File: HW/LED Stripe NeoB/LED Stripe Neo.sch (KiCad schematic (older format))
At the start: 22 parts, among them J1 IN-OUT, J2 IN-OUT, U1 WS2812B, U10 WS2812B, U2 WS2812B, U3 WS2812B, U4 WS2812B, U5 WS2812B, U6 WS2812B, U7 WS2812B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

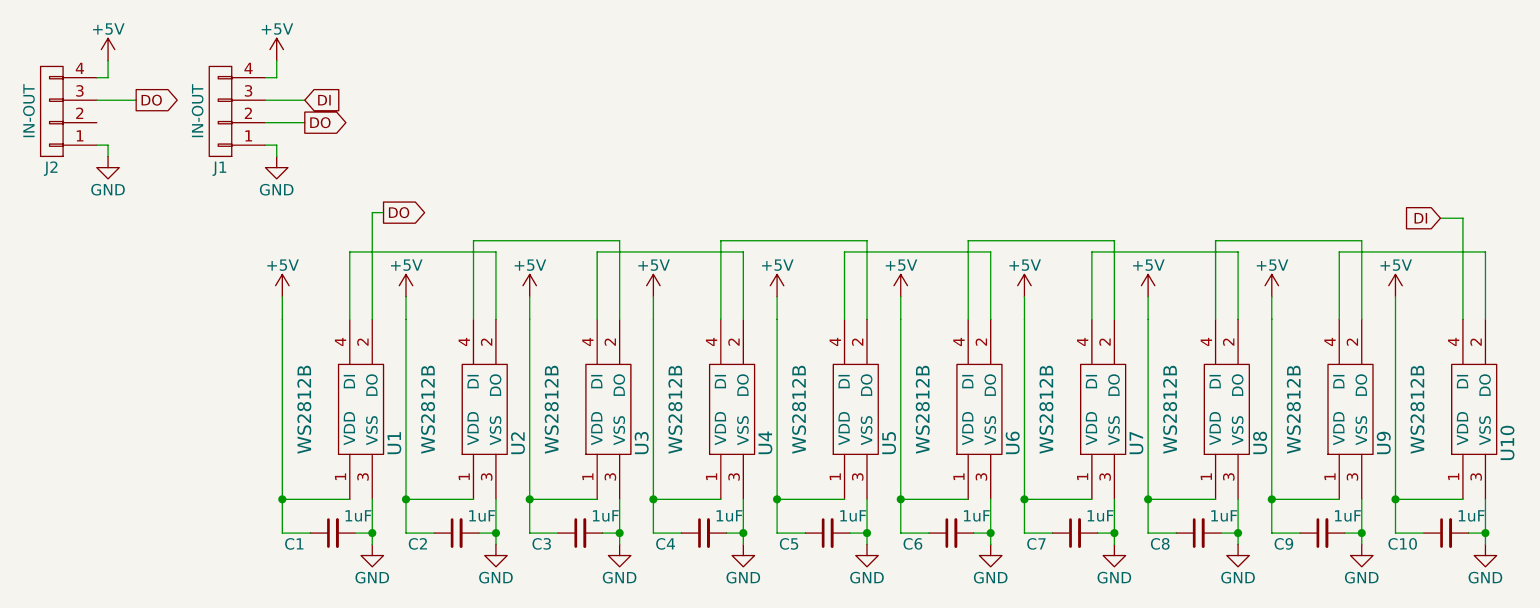
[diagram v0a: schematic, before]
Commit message: WS2812B SCH/PCB added
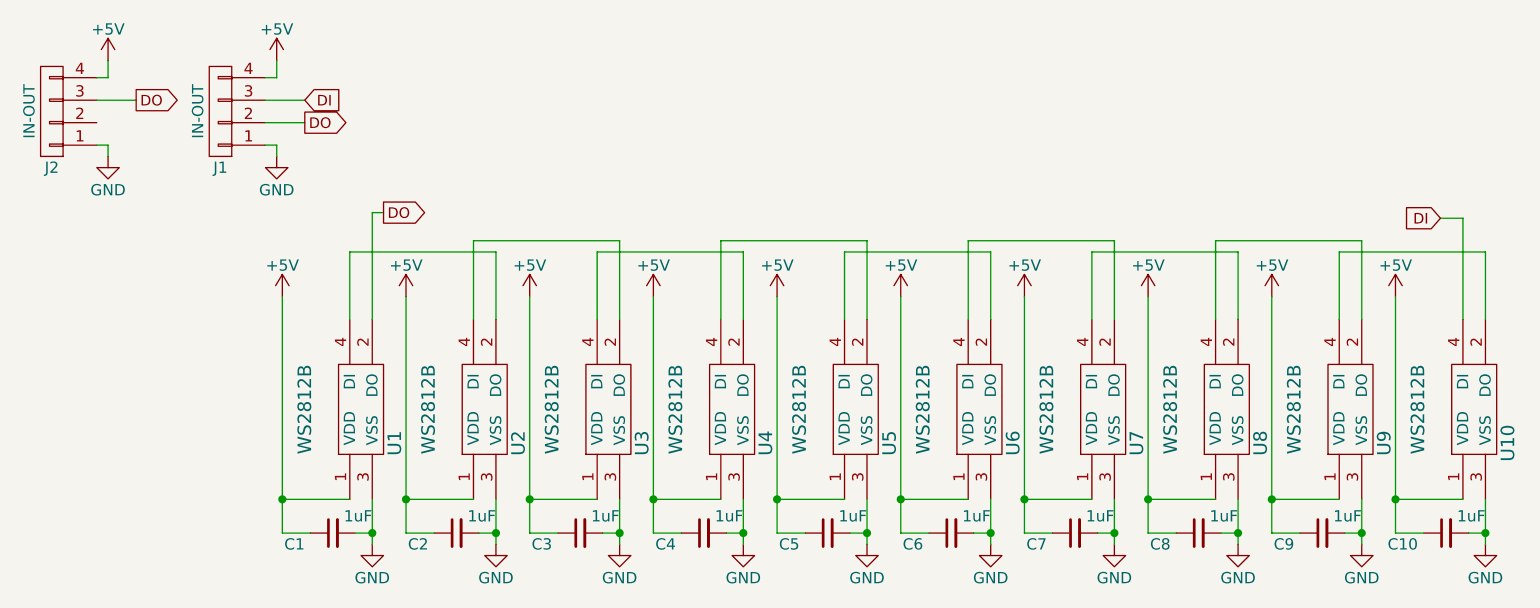
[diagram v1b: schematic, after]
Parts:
- U1, U10, U2, U3, U4, U5, U6, U7, U8, U9: footprint LEDs:LED-RGB_PLLC-6 -> suf_led:LED5050-WS2812B_HANDSOLDERING
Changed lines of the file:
@@
 LIBS:valves
 LIBS:suf_led
+LIBS:LED Stripe Neo-cache
 EELAYER 25 0
 EELAYER END
@@
 F 0 "U1" H 2000 2100 60  0000 C CNN
 F 1 "WS2812B" H 2150 2500 60  0000 C CNN
-F 2 "LEDs:LED-RGB_PLLC-6" H 2150 2300 60  0001 C CNN
+F 2 "suf_led:LED5050-WS2812B_HANDSOLDERING" H 2150 2300 60  0001 C CNN
 F 3 "" H 2150 2300 60  0000 C CNN
 	1    2150 2300
@@
 $EndComp
 Wire Wire Line
-	1850 1800 1850 1900
-Wire Wire Line
-	1850 1900 1850 2700
-Wire Wire Line
-	1850 2700 1850 2850
+	1850 1800 1850 2850
 Wire Wire Line
 	1850 2700 2150 2700
@@
 $EndComp
 Wire Wire Line
-	2250 2700 2250 2850
-Wire Wire Line
-	2250 2850 2250 2900
+	2250 2700 2250 2900
 Wire Wire Line
 	2175 2850 2250 2850
@@
 F 0 "U2" H 2550 2100 60  0000 C CNN
 F 1 "WS2812B" H 2700 2500 60  0000 C CNN
-F 2 "LEDs:LED-RGB_PLLC-6" H 2700 2300 60  0001 C CNN
+F 2 "suf_led:LED5050-WS2812B_HANDSOLDERING" H 2700 2300 60  0001 C CNN
 F 3 "" H 2700 2300 60  0000 C CNN
 	1    2700 2300
@@
 $EndComp
 Wire Wire Line
-	2400 1800 2400 1900
-Wire Wire Line
-	2400 1900 2400 2700
-Wire Wire Line
-	2400 2700 2400 2850
+	2400 1800 2400 2850
 Wire Wire Line
 	2400 2700 2700 2700
@@
 $EndComp
 Wire Wire Line
-	2800 2700 2800 2850
-Wire Wire Line
-	2800 2850 2800 2900
+	2800 2700 2800 2900
 Wire Wire Line
 	2725 2850 2800 2850
@@
 F 0 "U3" H 3100 2100 60  0000 C CNN
 F 1 "WS2812B" H 3250 2500 60  0000 C CNN
-F 2 "LEDs:LED-RGB_PLLC-6" H 3250 2300 60  0001 C CNN
+F 2 "suf_led:LED5050-WS2812B_HANDSOLDERING" H 3250 2300 60  0001 C CNN
 F 3 "" H 3250 2300 60  0000 C CNN
 	1    3250 2300
@@
 $EndComp
 Wire Wire Line
-	2950 1800 2950 1900
-Wire Wire Line
-	2950 1900 2950 2700
-Wire Wire Line
-	2950 2700 2950 2850
+	2950 1800 2950 2850
 Wire Wire Line
 	2950 2700 3250 2700
@@
 $EndComp
 Wire Wire Line
-	3350 2700 3350 2850
-Wire Wire Line
-	3350 2850 3350 2900
+	3350 2700 3350 2900
 Wire Wire Line
 	3275 2850 3350 2850
@@
 F 0 "U4" H 3650 2100 60  0000 C CNN
 F 1 "WS2812B" H 3800 2500 60  0000 C CNN
-F 2 "LEDs:LED-RGB_PLLC-6" H 3800 2300 60  0001 C CNN
+F 2 "suf_led:LED5050-WS2812B_HANDSOLDERING" H 3800 2300 60  0001 C CNN
 F 3 "" H 3800 2300 60  0000 C CNN
 	1    3800 2300
@@
 $EndComp
 Wire Wire Line
-	3500 1800 3500 1900
-Wire Wire Line
-	3500 1900 3500 2700
-Wire Wire Line
-	3500 2700 3500 2850
+	3500 1800 3500 2850
 Wire Wire Line
 	3500 2700 3800 2700
@@
 $EndComp
 Wire Wire Line
-	3900 2700 3900 2850
-Wire Wire Line
-	3900 2850 3900 2900
+	3900 2700 3900 2900
 Wire Wire Line
 	3825 2850 3900 2850
@@
 F 0 "U5" H 4200 2100 60  0000 C CNN
 F 1 "WS2812B" H 4350 2500 60  0000 C CNN
-F 2 "LEDs:LED-RGB_PLLC-6" H 4350 2300 60  0001 C CNN
+F 2 "suf_led:LED5050-WS2812B_HANDSOLDERING" H 4350 2300 60  0001 C CNN
 F 3 "" H 4350 2300 60  0000 C CNN
 	1    4350 2300
@@
 $EndComp
 Wire Wire Line
-	4050 1800 4050 1900
-Wire Wire Line
-	4050 1900 4050 2700
-Wire Wire Line
-	4050 2700 4050 2850
+	4050 1800 4050 2850
 Wire Wire Line
 	4050 2700 4350 2700
@@
 $EndComp
 Wire Wire Line
-	4450 2700 4450 2850
-Wire Wire Line
-	4450 2850 4450 2900
+	4450 2700 4450 2900
 Wire Wire Line
 	4375 2850 4450 2850
@@
 F 0 "U6" H 4750 2100 60  0000 C CNN
 F 1 "WS2812B" H 4900 2500 60  0000 C CNN
-F 2 "LEDs:LED-RGB_PLLC-6" H 4900 2300 60  0001 C CNN
+F 2 "suf_led:LED5050-WS2812B_HANDSOLDERING" H 4900 2300 60  0001 C CNN
 F 3 "" H 4900 2300 60  0000 C CNN
 	1    4900 2300
@@
 $EndComp
 Wire Wire Line
-	4600 1800 4600 1900
-Wire Wire Line
-	4600 1900 4600 2700
-Wire Wire Line
-	4600 2700 4600 2850
+	4600 1800 4600 2850
 Wire Wire Line
 	4600 2700 4900 2700
@@
 $EndComp
 Wire Wire Line
-	5000 2700 5000 2850
-Wire Wire Line
-	5000 2850 5000 2900
+	5000 2700 5000 2900
 Wire Wire Line
 	4925 2850 5000 2850
@@
 F 0 "U7" H 5300 2100 60  0000 C CNN
 F 1 "WS2812B" H 5450 2500 60  0000 C CNN
-F 2 "LEDs:LED-RGB_PLLC-6" H 5450 2300 60  0001 C CNN
+F 2 "suf_led:LED5050-WS2812B_HANDSOLDERING" H 5450 2300 60  0001 C CNN
 F 3 "" H 5450 2300 60  0000 C CNN
 	1    5450 2300
@@
 $EndComp
 Wire Wire Line
-	5150 1800 5150 1900
-Wire Wire Line
-	5150 1900 5150 2700
-Wire Wire Line
-	5150 2700 5150 2850
+	5150 1800 5150 2850
 Wire Wire Line
 	5150 2700 5450 2700
@@
 $EndComp
 Wire Wire Line
-	5550 2700 5550 2850
-Wire Wire Line
-	5550 2850 5550 2900
+	5550 2700 5550 2900
 Wire Wire Line
 	5475 2850 5550 2850
@@
 F 0 "U8" H 5850 2100 60  0000 C CNN
 F 1 "WS2812B" H 6000 2500 60  0000 C CNN
-F 2 "LEDs:LED-RGB_PLLC-6" H 6000 2300 60  0001 C CNN
+F 2 "suf_led:LED5050-WS2812B_HANDSOLDERING" H 6000 2300 60  0001 C CNN
 F 3 "" H 6000 2300 60  0000 C CNN
 	1    6000 2300
@@
 $EndComp
 Wire Wire Line
-	5700 1800 5700 1900
-Wire Wire Line
-	5700 1900 5700 2700
-Wire Wire Line
-	5700 2700 5700 2850
+	5700 1800 5700 2850
 Wire Wire Line
 	5700 2700 6000 2700
@@
 $EndComp
 Wire Wire Line
-	6100 2700 6100 2850
-Wire Wire Line
-	6100 2850 6100 2900
+	6100 2700 6100 2900
 Wire Wire Line
 	6025 2850 6100 2850
@@
 F 0 "U9" H 6400 2100 60  0000 C CNN
 F 1 "WS2812B" H 6550 2500 60  0000 C CNN
-F 2 "LEDs:LED-RGB_PLLC-6" H 6550 2300 60  0001 C CNN
+F 2 "suf_led:LED5050-WS2812B_HANDSOLDERING" H 6550 2300 60  0001 C CNN
 F 3 "" H 6550 2300 60  0000 C CNN
 	1    6550 2300
@@
 $EndComp
 Wire Wire Line
-	6250 1800 6250 1900
-Wire Wire Line
-	6250 1900 6250 2700
-Wire Wire Line
-	6250 2700 6250 2850
+	6250 1800 6250 2850
 Wire Wire Line
 	6250 2700 6550 2700
@@
 $EndComp
 Wire Wire Line
-	6650 2700 6650 2850
-Wire Wire Line
-	6650 2850 6650 2900
+	6650 2700 6650 2900
 Wire Wire Line
 	6575 2850 6650 2850
@@
 F 0 "U10" H 6950 2100 60  0000 C CNN
 F 1 "WS2812B" H 7100 2500 60  0000 C CNN
-F 2 "LEDs:LED-RGB_PLLC-6" H 7100 2300 60  0001 C CNN
+F 2 "suf_led:LED5050-WS2812B_HANDSOLDERING" H 7100 2300 60  0001 C CNN
 F 3 "" H 7100 2300 60  0000 C CNN
 	1    7100 2300
@@
 $EndComp
 Wire Wire Line
-	6800 1800 6800 1900
-Wire Wire Line
-	6800 1900 6800 2700
-Wire Wire Line
-	6800 2700 6800 2850
+	6800 1800 6800 2850
 Wire Wire Line
 	6800 2700 7100 2700
@@
 $EndComp
 Wire Wire Line
-	7200 2700 7200 2850
-Wire Wire Line
-	7200 2850 7200 2900
+	7200 2700 7200 2900
 Wire Wire Line
 	7125 2850 7200 2850
